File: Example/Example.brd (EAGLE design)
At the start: 86 x 54 mm, 21 parts, among them IC1 LM555D, IC2 74LS02D, IC3 74LS02D, J1 UX60-MB-5S8, SW1 MFS101D-6-Z

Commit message: Added CD4017 Decade Counter
Part can be found in the SparkFun-IC-Logiv Library
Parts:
- added U1: CD4017, SparkFun-IC-Logic:DIP16
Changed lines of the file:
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@@
 <attribute name="VALUE" x="-25.688" y="-84.33" size="1.6764" layer="27" font="vector"/>
+</element>
+<element name="U1" library="SparkFun-IC-Logic" library_urn="urn:adsk.eagle:library:523" package="DIP16" package3d_urn="urn:adsk.eagle:package:38809/1" value="CD4017" x="-19.57" y="-91.13" smashed="yes">
+<attribute name="NAME" x="-30.365" y="-91.13" size="0.6096" layer="25" font="vector" ratio="20" rot="R90" align="bottom-center"/>
+<attribute name="PROD_ID" value="IC-11929" x="-19.57" y="-91.13" size="1.778" layer="27" display="off"/>
+<attribute name="VALUE" x="-8.14" y="-91.13" size="0.6096" layer="27" font="vector" ratio="20" rot="R90" align="bottom-center"/>
 </element>
 </elements>

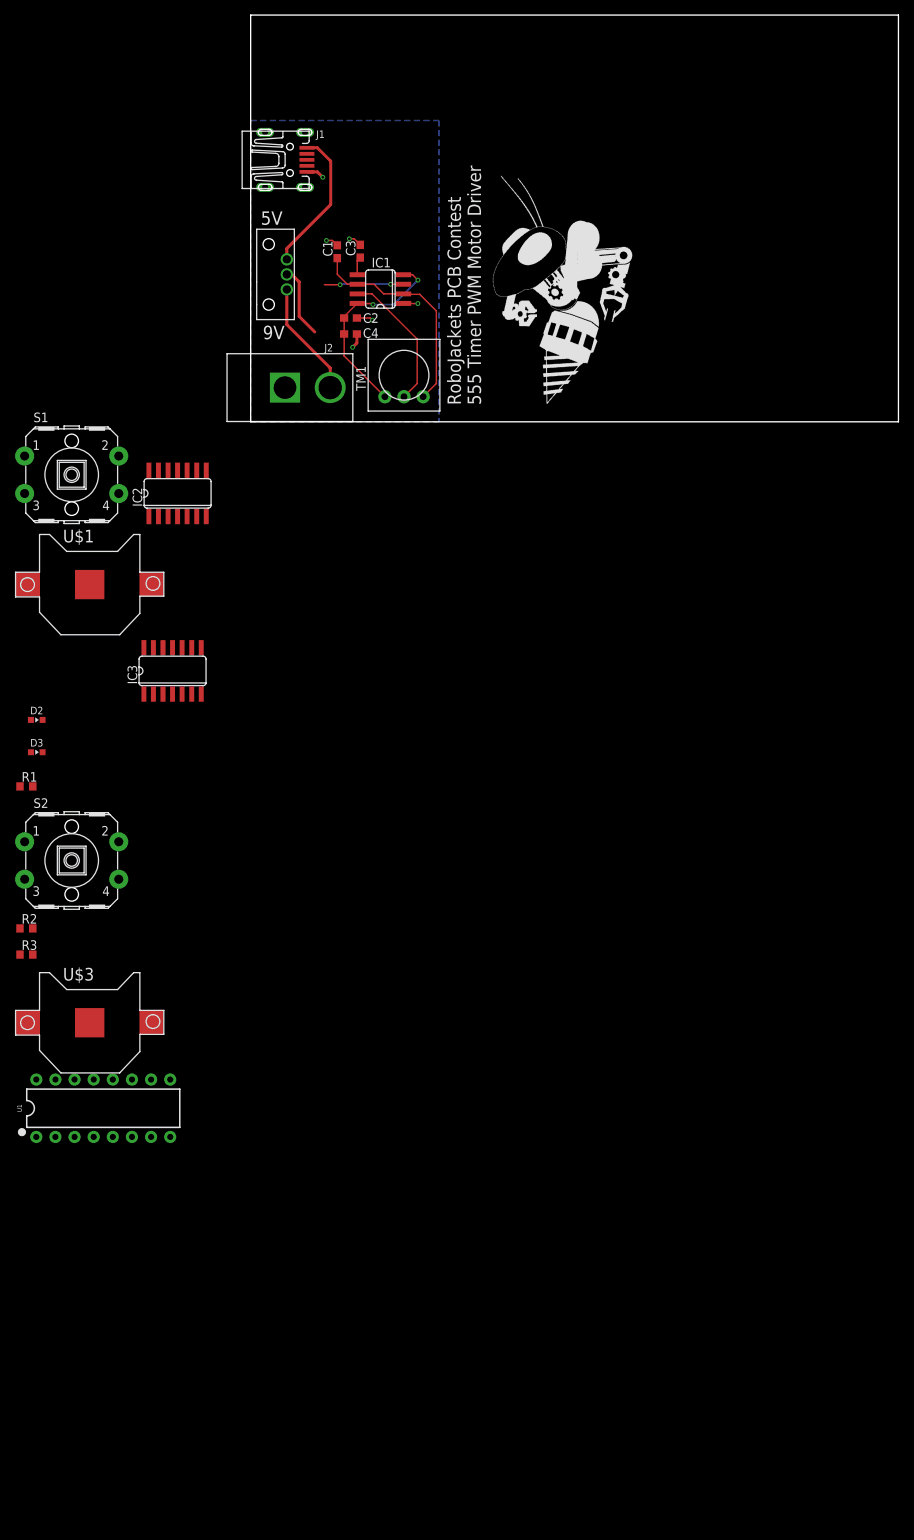
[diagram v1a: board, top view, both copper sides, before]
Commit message: decade counter
leds for decade counter
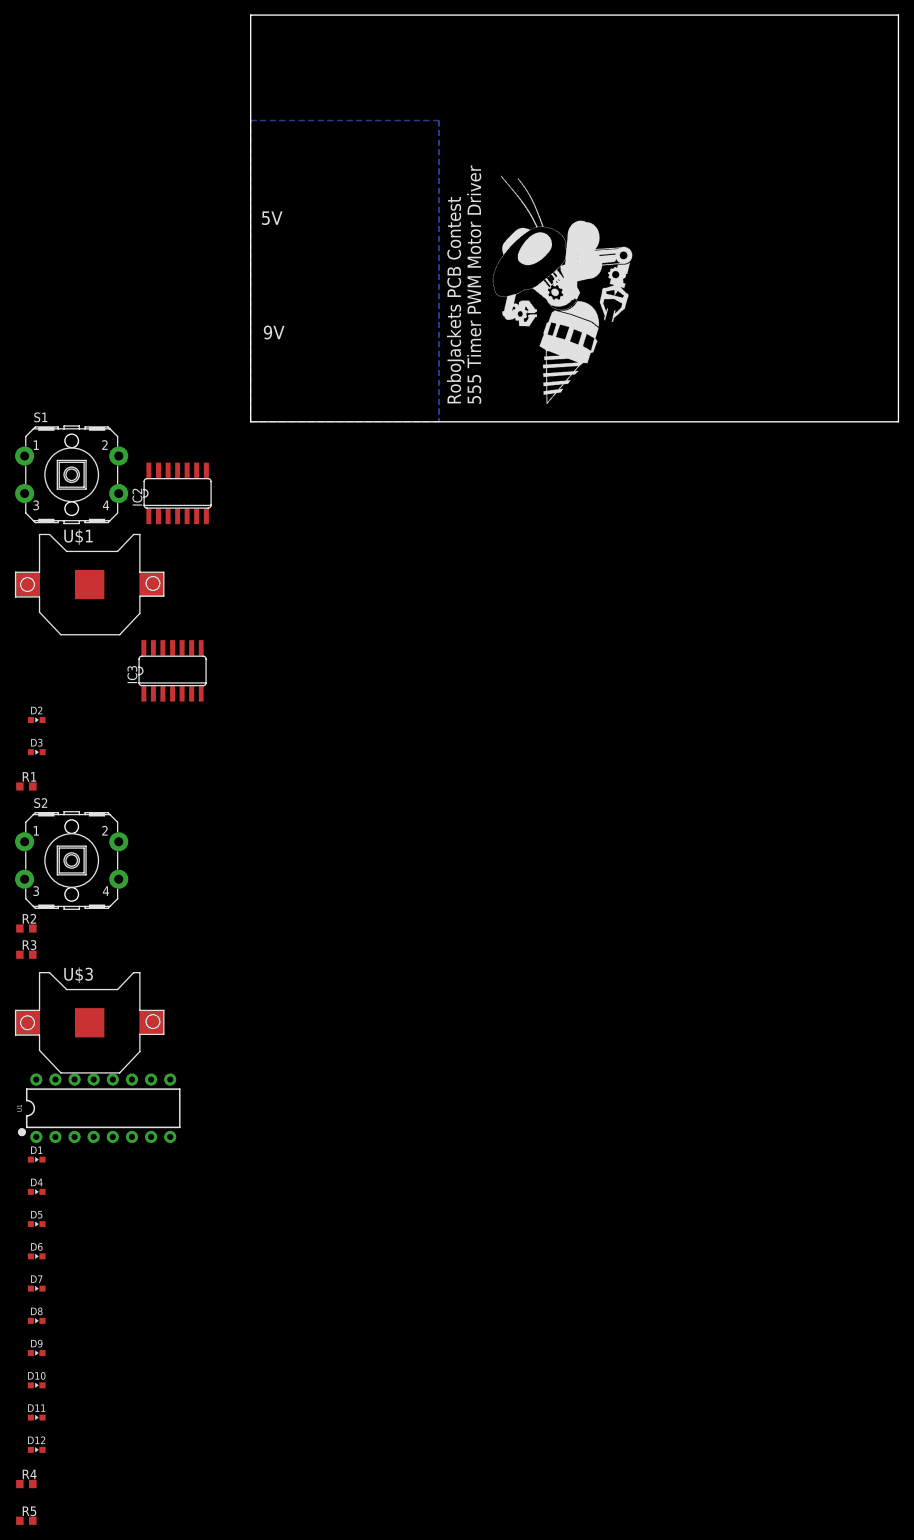
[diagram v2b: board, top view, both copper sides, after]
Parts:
- removed C1, C3: 0.01uF, rcl:C0603
- removed C2: 0.1uF, rcl:C0603
- removed C4: 10uF, rcl:C0603
- removed IC1: LM555D, adafruit:SO08
- removed J1: UX60-MB-5S8, RoboJackets-Connectors:UX60-MB-5S8
- removed J2: (no value), RoboJackets-Connectors:PJ-037A
- removed SW1: MFS101D-6-Z, Example:MFS101D-6-Z
- removed TM1: (no value), adafruit:TRIM-3386
- added D1, D10, D11, D12, D4, D5, D6, D7, D8, D9: YELLOW, RoboJackets-LEDs:LED0603
- added R4: 2200, rcl:R0603
- added R5: 220, rcl:R0603
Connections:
- removed net +9V: C2.1, C4.1, IC1.4, IC1.8, SW1.2, TM1.1
- removed net N$1: IC1.7, TM1.2
- removed net N$3: C3.1, IC1.5
- removed net N$4: J1.1, SW1.3
- removed net N$6: J2.P$2, SW1.1
- removed net THR: C1.1, IC1.2, IC1.6, TM1.3
- removed net T_OUT: IC1.3
- new net N$10: D1.A, U1.3
- new net N$11: D4.A, U1.2
- new net N$12: D5.A, U1.4
- new net N$13: D6.A, U1.7
- new net N$14: D7.A, U1.10
- new net N$15: D8.A, U1.1
- new net N$16: D9.A, U1.5
- new net N$17: D10.A, U1.6
- new net N$18: D11.A, U1.9
- new net N$19: D12.A, U1.11
- new net N$20: D1.C, D10.C, D11.C, D12.C, D4.C, D5.C, D6.C, D7.C, D8.C, D9.C, R4.2
- new net N$21: R5.2, U1.15
- net GND: now also R4.1, R5.1; no longer C1.2, C2.2, C3.2, C4.2, IC1.1, J1.5, J2.P$1
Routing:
- net +9V: track 37.0 -> 0.00 mm, vias 2 -> 0
- net THR: track 29.4 -> 0.00 mm
- net N$4: track 19.3 -> 0.00 mm
- net N$1: track 18.8 -> 0.00 mm
- net N$6: track 15.4 -> 0.00 mm
- net GND: track 12.0 -> 0.00 mm, vias 6 -> 0
- net T_OUT: track 10.5 -> 0.00 mm, vias 2 -> 0
- net N$3: track 2.43 -> 0.00 mm
